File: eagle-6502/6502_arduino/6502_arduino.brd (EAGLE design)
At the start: 76.2 x 53.3 mm, 40 parts, among them U1 UM6507, U2 R6532, U3 28C256, U4 MCP2221-I/SL, U5 LFSPXO058610, U6 74HC00D, U7 74HC138D, X1 ARDUINO_UNO_PINS, X2 TACT_SWITCH, X3 TACT_SWITCH, X4 USB-B

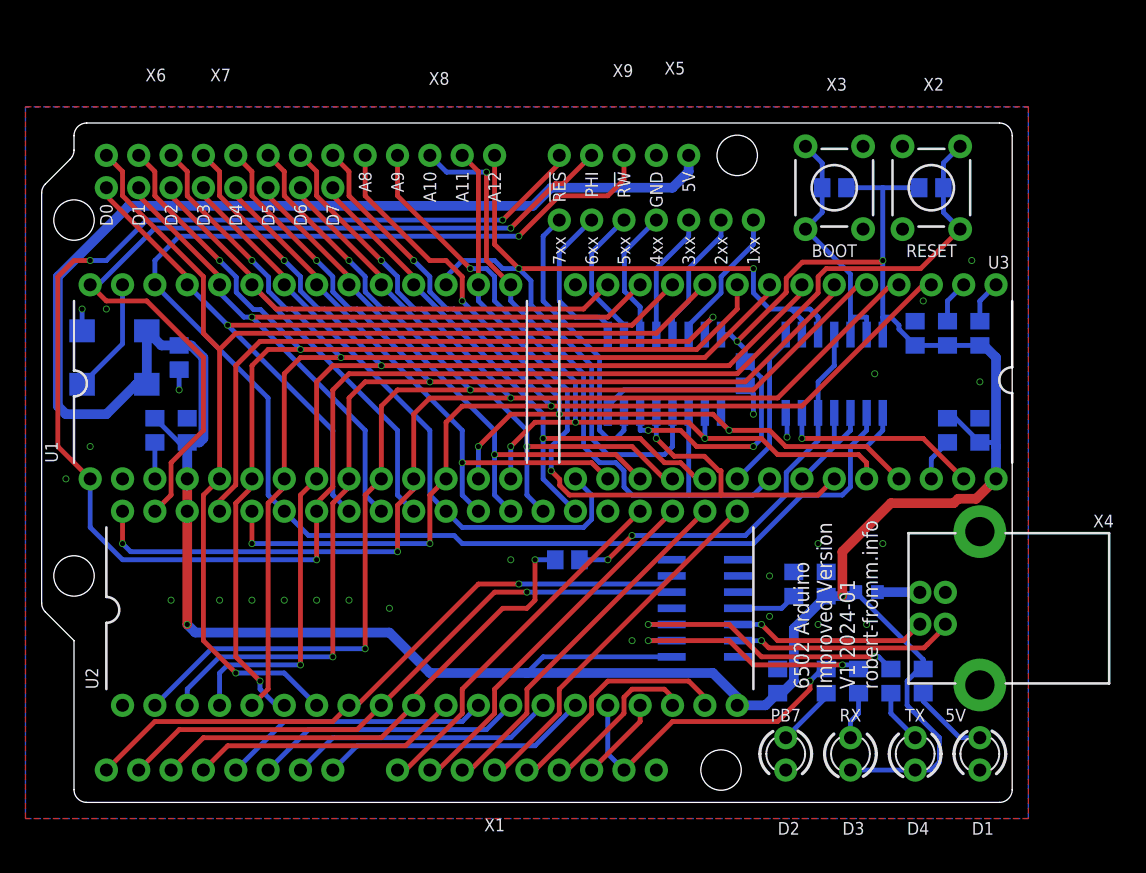
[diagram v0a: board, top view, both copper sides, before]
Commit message: Tested PCB design on breadboard, added BAT54A ORing on 74x138 lines to allow stack served by RIOT, ORing of UART status LEDs
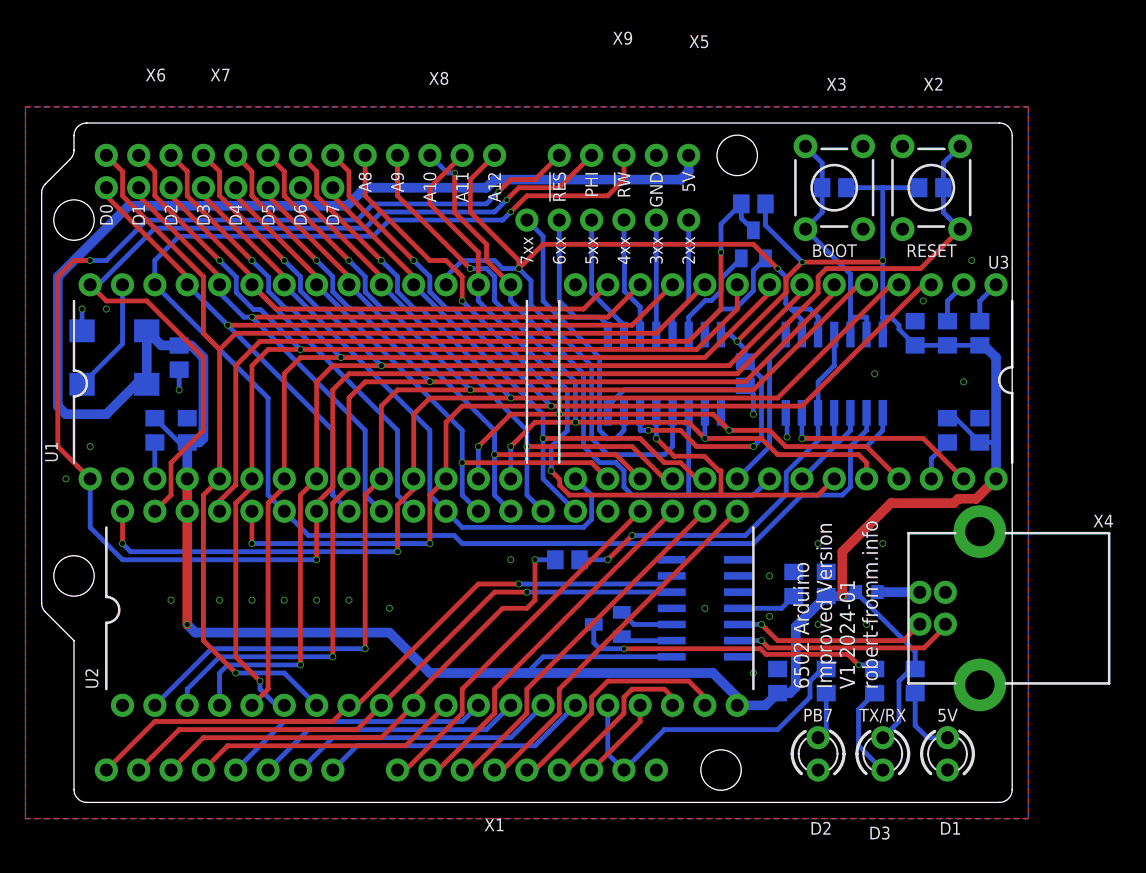
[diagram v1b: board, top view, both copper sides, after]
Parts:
- added D5: BAT54A, diode:SOT23
- D4: value (none) -> BAT54A; device 6502_lib:LED3MM -> diode:SOT23
- X5: device 6502_lib:1X07 -> 6502_lib:1X06
- moved D4 42.0 mm to (55.9, 43.8), flipped to the bottom, turned to 0 degrees
- moved R11 39.0 mm to (55.9, 47.0), turned to 180 degrees
- moved X5 3.81 mm to (44.5, 45.7)
- moved D3 2.54 mm to (66.0, 3.81), turned to 270 degrees
- moved D2 2.54 mm to (61.0, 3.81)
- moved D1 2.54 mm to (71.1, 3.81)
- moved R10 1.27 mm to (65.4, 9.53)
- moved R6 0.64 mm to (68.6, 9.53)
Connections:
- removed net !CS!_0100: U7.14, X5.1
- new net N$13: D4.1, U7.15
- new net N$17: D4.2, U7.14
- net !CS!_0200: now also X5.1; no longer X5.2
- net !CS!_0300: now also X5.2; no longer X5.3
- net !CS!_0400: now also X5.3; no longer X5.4
- net !CS!_0500: now also X5.4; no longer X5.5
- net !CS!_0600: now also X5.5; no longer X5.6
- net !CS!_0700: now also X5.6; no longer X5.7
- net +5V: now also R11.2; no longer D4.A
- net N$10: now also D5.3, R10.2; no longer D4.K, R11.1
- net RIOT_!CS: now also D4.3, R11.1; no longer U7.15
- net RX_STATUS: now also D5.2; no longer R10.2
- net TX_STATUS: now also D5.1; no longer R11.2
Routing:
- net N$10: track 4.28 -> 24.3 mm, vias 0 -> 2
- net TX_STATUS: track 22.3 -> 4.31 mm, vias 2 -> 0
- net RX_STATUS: track 19.3 -> 4.05 mm, vias 2 -> 0
- net !CS!_0100: track 11.1 -> 0.00 mm
- net RIOT_!CS: track 52.6 -> 63.3 mm
- net N$13: track 0.00 -> 8.61 mm
- net N$17: track 0.00 -> 7.97 mm
- net +5V: track 301.8 -> 297.8 mm, vias 6 -> 7
- net N$8: track 3.76 -> 7.35 mm
- net A12: track 72.2 -> 75.5 mm
- net A11: track 62.6 -> 64.7 mm
- net A10: track 53.6 -> 52.3 mm
- net !CS!_0200: track 10.6 -> 9.52 mm
- net !CS!_0600: track 12.7 -> 11.7 mm
- net !CS!_0500: track 11.1 -> 10.0 mm
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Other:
- board text added: "TX/RX"
- board text removed: "1xx"
- board text removed: "RX"
- board text removed: "TX"
